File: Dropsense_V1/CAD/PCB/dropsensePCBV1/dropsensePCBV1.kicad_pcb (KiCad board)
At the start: 2 copper layers, 26 parts, among them J1 Micro_SD_Card_Det_Hirose_DM3AT, J2 USB_B_Micro, J3 Conn_01x02_Socket, SW1 SW_Push, SW2 SW_Push, U1 ESP32-S3-WROOM-1, U2 MPU-6050, U3 TP4056-42-ESOP8, U4 ME6211C10M5

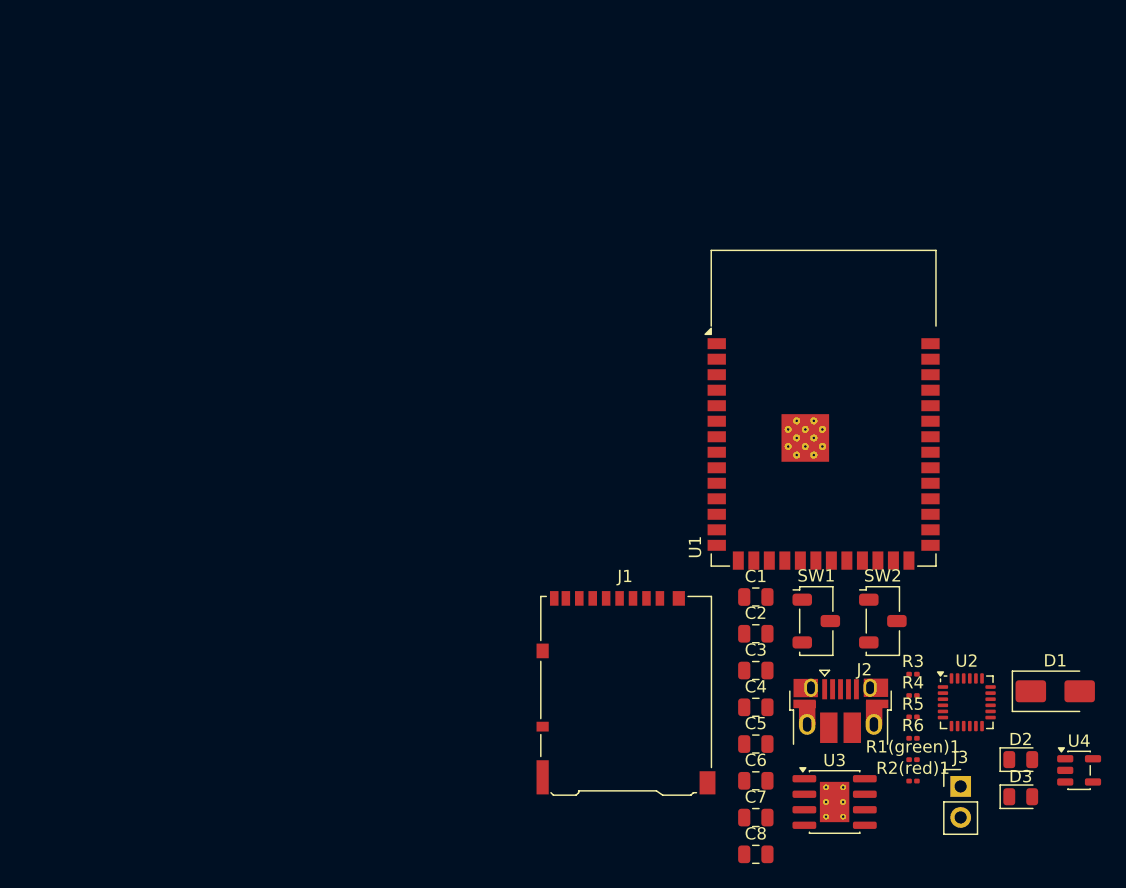
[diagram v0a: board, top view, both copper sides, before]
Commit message: UPDATED DROPSENSE PCB
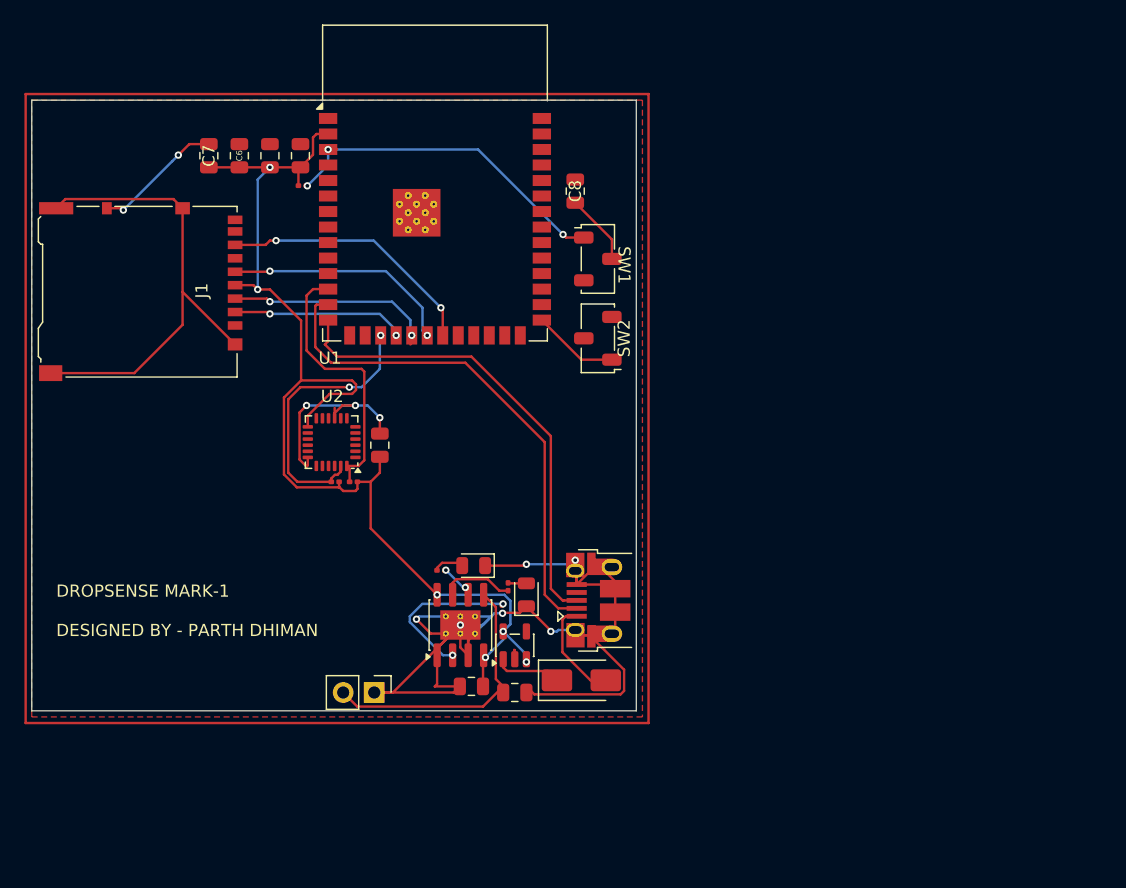
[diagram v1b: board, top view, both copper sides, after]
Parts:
- D2: value LED -> green
- D3: value LED -> red
- J3: value Conn_01x02_Socket -> battery socket
- moved C7 70.3 mm to (94.0, 54.5), turned to -90 degrees
- moved R6 67.4 mm to (101.7, 57.0)
- moved C6 66.4 mm to (96.5, 54.5), turned to 90 degrees
- moved C5 62.5 mm to (99.0, 54.5), turned to 90 degrees
- moved C4 58.6 mm to (101.5, 54.5), turned to 90 degrees
- moved C8 56.3 mm to (124.0, 57.5), turned to 90 degrees
- moved U2 56.2 mm to (104.0, 78.0), turned to 180 degrees
- moved J1 51.5 mm to (88.4, 65.7), turned to -90 degrees
- moved R4 50.4 mm to (104.3, 81.2), turned to 180 degrees
- moved R5 49.7 mm to (105.8, 81.2), turned to 180 degrees
- moved J3 48.6 mm to (107.5, 98.5), turned to -90 degrees
- moved D3 48.6 mm to (115.7, 88.1), turned to 180 degrees
- moved U4 47.3 mm to (119.0, 94.6), turned to 90 degrees
- moved D2 42.7 mm to (120.0, 90.5), turned to 90 degrees
- moved R2 42.3 mm to (113.0, 88.5), turned to 180 degrees
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- renumbered R1(green)1 to R1, R2(red)1 to R2
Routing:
- net GND: track 0.00 -> 133.3 mm, vias 0 -> 11
- net 3v3: track 0.00 -> 94.7 mm, vias 0 -> 6
- net gpio20: track 0.00 -> 42.1 mm
- net unconnected-(J1-SHIELD-Pad11): track 0.00 -> 39.0 mm
- net gpio19: track 0.00 -> 38.8 mm
- net Net-(U1-EN): track 0.00 -> 27.8 mm, vias 0 -> 3
- net SCL: track 0.00 -> 22.9 mm, vias 0 -> 2
- net /+ve: track 0.00 -> 22.4 mm
- net SDA: track 0.00 -> 22.2 mm
- net MISO: track 0.00 -> 21.6 mm, vias 0 -> 2
- net SCk: track 0.00 -> 19.0 mm, vias 0 -> 2
- net MOSI: track 0.00 -> 17.3 mm, vias 0 -> 2
- net gpio10: track 0.00 -> 14.4 mm, vias 0 -> 2
- net Net-(U3-PROG): track 0.00 -> 13.9 mm, vias 0 -> 2
- net Net-(D1-A): track 0.00 -> 8.46 mm
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- added copper zone on F.Cu, net GND
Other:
- board outline added: 49.5 x 50 mm
- board text added: "C5"
- board text added: "DROPSENSE MARK-1 DESIGNED BY - PARTH DHIMAN"
